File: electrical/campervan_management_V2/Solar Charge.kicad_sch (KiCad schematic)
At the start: 23 parts, among them Q3 FDS4685, Q4 FDS4685, U1 MCP16311x-xMNY, U12 LTV-817S-TA1-C, U7 LTV-817S-TA1-C

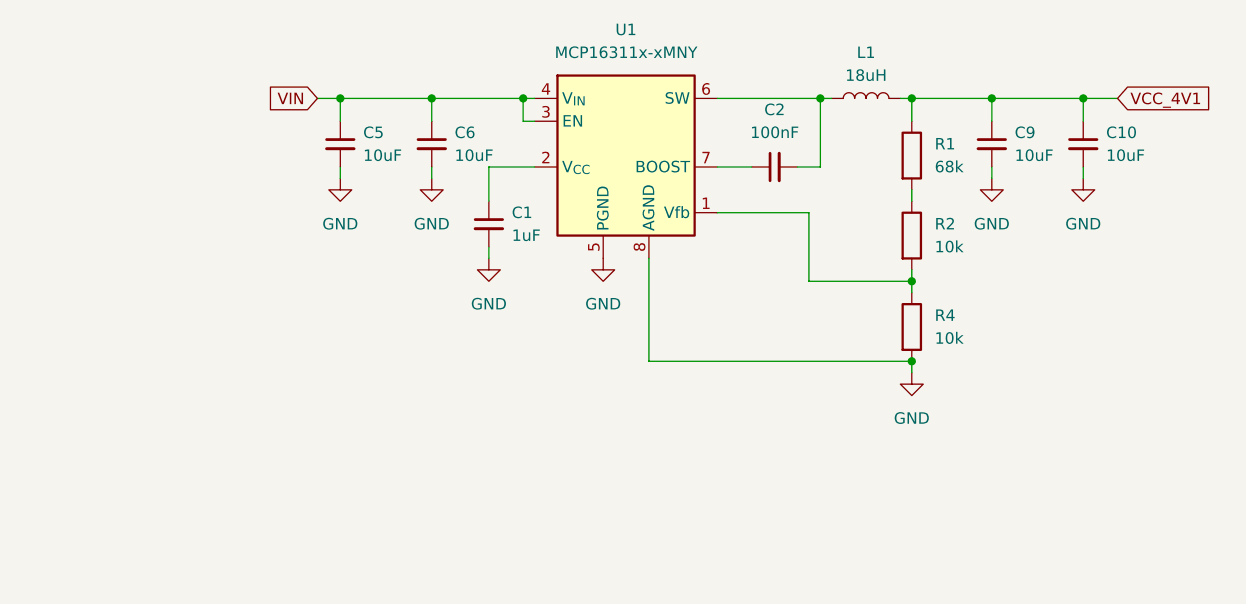
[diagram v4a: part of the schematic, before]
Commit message: updated 4V1 switcher resistor values. Clean up and reannotate PCB
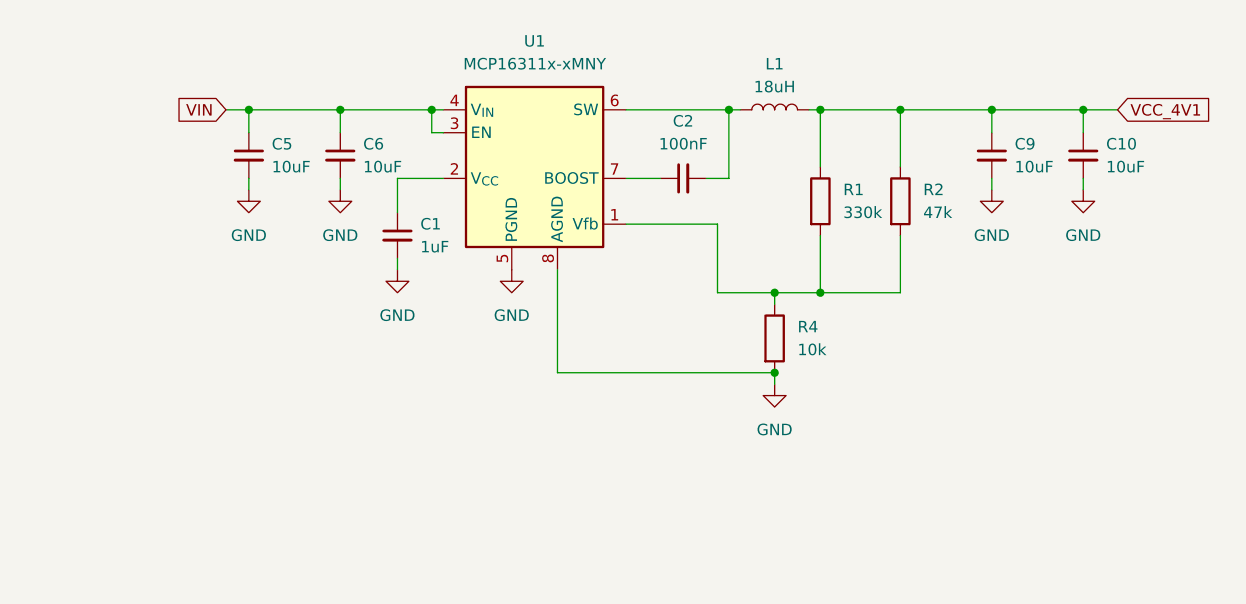
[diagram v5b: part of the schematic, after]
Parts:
- R1: value 68k -> 330k
- R2: value 10k -> 47k
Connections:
- net VCC_4V1: now also R2.1
- net at R1.2: now also R2.2, R4.1, U1.1 (Vfb); no longer R2.1
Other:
- moved on the sheet: C1, C10, C2, C5, C6, C9, L1, R1, R2, R4, U1
